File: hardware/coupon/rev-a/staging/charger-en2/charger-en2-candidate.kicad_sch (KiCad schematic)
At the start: 2 parts, among them U38 3V shunt

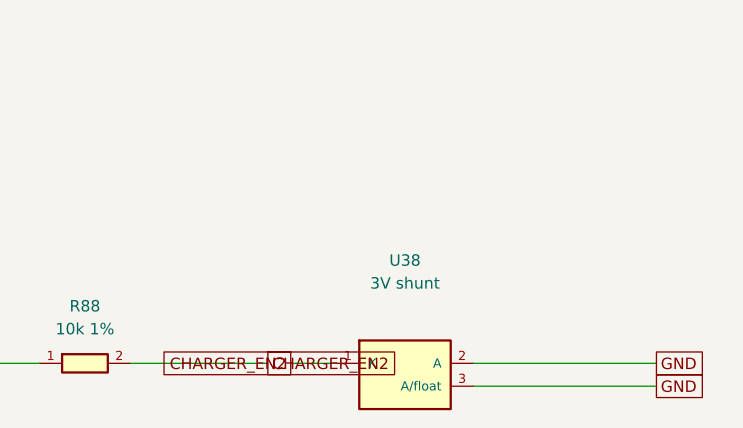
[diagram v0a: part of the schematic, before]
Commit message: Screen connectorized pack fit and refine EN2 clamp candidate
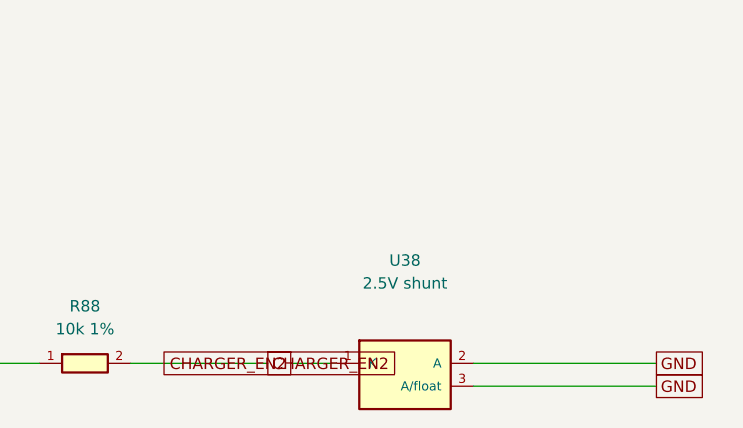
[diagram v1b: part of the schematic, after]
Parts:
- U38: value 3V shunt -> 2.5V shunt; symbol rgb-badge-coupon:LM4040A30IDBZT -> rgb-badge-coupon:LM4040A25IDBZT; MPN LM4040A30IDBZT -> LM4040A25IDBZT
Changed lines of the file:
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@@
 (pin "2")
 (instances (project "rgb-badge-coupon" (path "/b5a38eb6-fb94-5ba8-9658-31abc47a8fd9" (reference "R88") (unit 1)))))
-(symbol (lib_id "rgb-badge-coupon:LM4040A30IDBZT") (at 111.760 80.010 0) (unit 1)
+(symbol (lib_id "rgb-badge-coupon:LM4040A25IDBZT") (at 111.760 80.010 0) (unit 1)
 (exclude_from_sim no) (in_bom yes) (on_board yes) (dnp no)
 (property "Reference" "U38" (at 111.760 68.580 0) (effects (font (size 1.27 1.27))))
-(property "Value" "3V shunt" (at 111.760 71.120 0) (effects (font (size 1.27 1.27))))
+(property "Value" "2.5V shunt" (at 111.760 71.120 0) (effects (font (size 1.27 1.27))))
 (property "Footprint" "rgb-badge-coupon:SOT23_TI_DBZ0003A" (at 111.760 80.010 0) (effects (font (size 1.27 1.27)) (hide yes)))
 (property "Datasheet" "https://www.ti.com/lit/ds/symlink/lm4040.pdf" (at 111.760 80.010 0) (effects (font (size 1.27 1.27)) (hide yes)))
 (property "Manufacturer" "Texas Instruments" (at 111.760 80.010 0) (effects (font (size 1.27 1.27)) (hide yes)))
-(property "MPN" "LM4040A30IDBZT" (at 111.760 80.010 0) (effects (font (size 1.27 1.27)) (hide yes)))
+(property "MPN" "LM4040A25IDBZT" (at 111.760 80.010 0) (effects (font (size 1.27 1.27)) (hide yes)))
 (pin "1")
 (pin "2")
